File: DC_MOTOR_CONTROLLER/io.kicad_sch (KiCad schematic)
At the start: 12 parts, among them SW1 PEC12R, U1 NHD-C12832A1Z-FSRGB

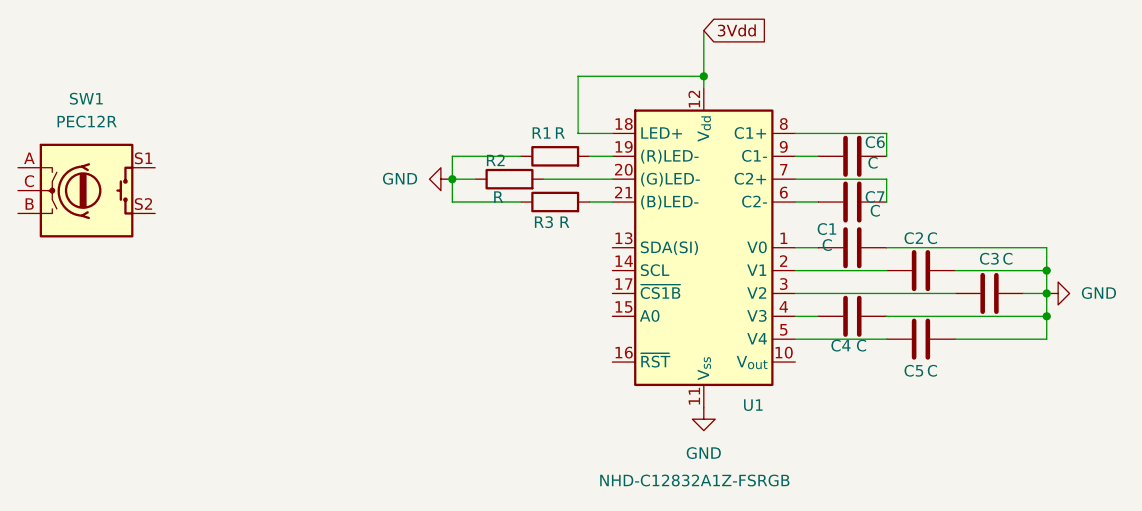
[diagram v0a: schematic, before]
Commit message: worked on h-bridge, pwm, io
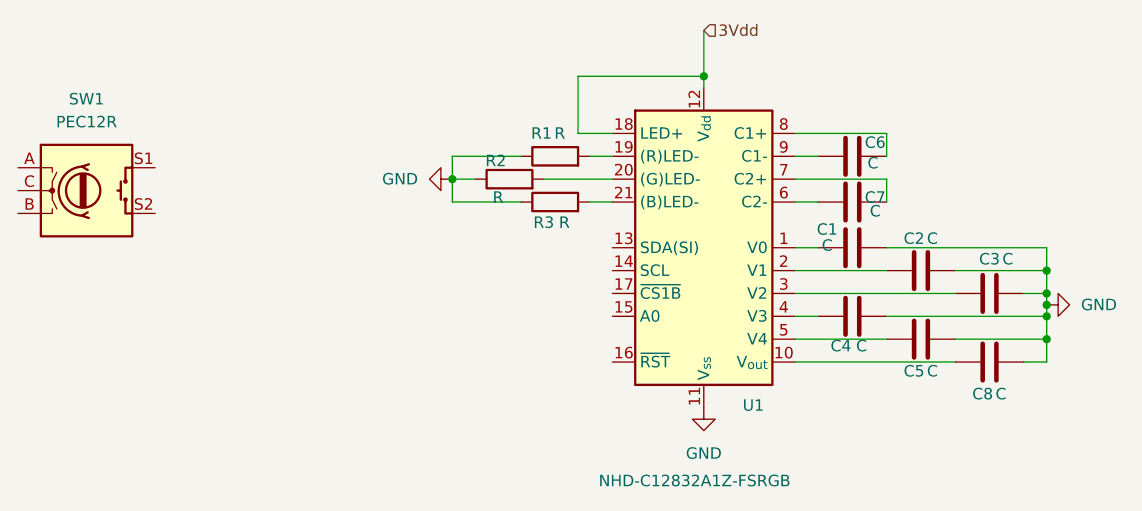
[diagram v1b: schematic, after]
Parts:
- added C8: C, symbol Device:C
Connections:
- net GND: now also C8.2
- net at U1.10 (V_{out}): now also C8.1
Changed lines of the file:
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@@
+	)
+	(junction
+		(at 190.5 80.01)
+		(diameter 0)
+		(color 0 0 0 0)
 	)
 	(junction
@@
 	)
 	(junction
+		(at 190.5 83.82)
+		(diameter 0)
+		(color 0 0 0 0)
+	)
+	(junction
 		(at 190.5 81.28)
 		(diameter 0)
@@
 	(wire
 		(pts
-			(xy 190.5 81.28) (xy 190.5 78.74)
+			(xy 190.5 81.28) (xy 190.5 80.01)
 		)
 		(stroke
@@
 	(wire
 		(pts
+			(xy 162.56 86.36) (xy 180.34 86.36)
+		)
+		(stroke
+			(width 0)
+			(type default)
+		)
+	)
+	(wire
+		(pts
+			(xy 190.5 86.36) (xy 190.5 83.82)
+		)
+		(stroke
+			(width 0)
+			(type default)
+		)
+	)
+	(wire
+		(pts
 			(xy 190.5 73.66) (xy 190.5 76.2)
 		)
@@
 	(wire
 		(pts
+			(xy 190.5 80.01) (xy 190.5 78.74)
+		)
+		(stroke
+			(width 0)
+			(type default)
+		)
+	)
+	(wire
+		(pts
 			(xy 152.4 54.61) (xy 152.4 55.88)
 		)
@@
 		)
 	)
-	(global_label "3Vdd"
+	(wire
+		(pts
+			(xy 187.96 86.36) (xy 190.5 86.36)
+		)
+		(stroke
+			(width 0)
+			(type default)
+		)
+	)
+	(hierarchical_label "3Vdd"
 		(shape input)
 		(at 152.4 49.53 0)
-		(fields_autoplaced yes)
 		(effects
 			(font
@@
 			)
 			(justify left)
-		)
-		(property "Intersheetrefs" "${INTERSHEET_REFS}"
-			(at 159.9813 49.53 0)
-			(effects
-				(font
-					(size 1.27 1.27)
-				)
-				(justify left)
-				(hide yes)
-			)
 		)
 	)
@@
 	)
 	(symbol
-		(lib_id "power:GND")
-		(at 190.5 78.74 90)
-		(unit 1)
-		(exclude_from_sim no)
-		(in_bom yes)
-		(on_board yes)
-		(dnp no)
-		(fields_autoplaced yes)
-		(property "Reference" "#PWR01"
-			(at 196.85 78.74 0)
-			(effects
-				(font
-					(size 1.27 1.27)
-				)
-				(hide yes)
-			)
-		)
-		(property "Value" "GND"
-			(at 194.31 78.7399 90)
-			(effects
-				(font
-					(size 1.27 1.27)
-				)
-				(justify right)
-			)
-		)
-		(property "Footprint" ""
-			(at 190.5 78.74 0)
-			(effects
-				(font
-					(size 1.27 1.27)
-				)
-				(hide yes)
-			)
-		)
-		(property "Datasheet" ""
-			(at 190.5 78.74 0)
-			(effects
-				(font
-					(size 1.27 1.27)
-				)
-				(hide yes)
-			)
-		)
-		(property "Description" "Power symbol creates a global label with name \"GND\" , ground"
-			(at 190.5 78.74 0)
-			(effects
-				(font
-					(size 1.27 1.27)
-				)
-				(hide yes)
-			)
-		)
-		(pin "1"
-		)
-		(instances
-			(project ""
-				(path "/4e267608-d3e9-4ae4-92d6-1e687cc2c969/818b61c9-cdb7-42ed-8a55-79736ba5dd65"
-					(reference "#PWR01")
-					(unit 1)
-				)
-			)
-		)
-	)
-	(symbol
 		(lib_id "Device:C")
 		(at 168.91 63.5 90)
@@
 				(path "/4e267608-d3e9-4ae4-92d6-1e687cc2c969/818b61c9-cdb7-42ed-8a55-79736ba5dd65"
 					(reference "C6")
+					(unit 1)
+				)
+			)
+		)
+	)
+	(symbol
+		(lib_id "Device:C")
+		(at 184.15 86.36 90)
+		(unit 1)
+		(exclude_from_sim no)
+		(in_bom yes)
+		(on_board yes)
+		(dnp no)
+		(property "Reference" "C8"
+			(at 183.388 89.916 90)
+			(effects
+				(font
+					(size 1.27 1.27)
+				)
+			)
+		)
+		(property "Value" "C"
+			(at 185.42 89.916 90)
+			(effects
+				(font
+					(size 1.27 1.27)
+				)
+			)
+		)
+		(property "Footprint" ""
+			(at 187.96 85.3948 0)
+			(effects
+				(font
+					(size 1.27 1.27)
+				)
+				(hide yes)
+			)
+		)
+		(property "Datasheet" "~"
+			(at 184.15 86.36 0)
+			(effects
+				(font
+					(size 1.27 1.27)
+				)
+				(hide yes)
+			)
+		)
+		(property "Description" "Unpolarized capacitor"
+			(at 184.15 86.36 0)
+			(effects
+				(font
+					(size 1.27 1.27)
+				)
+				(hide yes)
+			)
+		)
+		(pin "2"
+		)
+		(pin "1"
+		)
+		(instances
+			(project "DC_MOTOR_CONTROLLER"
+				(path "/4e267608-d3e9-4ae4-92d6-1e687cc2c969/818b61c9-cdb7-42ed-8a55-79736ba5dd65"
+					(reference "C8")
 					(unit 1)
 				)
@@
 					(unit 1)
 				)
+			)
+		)
+	)
+	(symbol
+		(lib_id "power:GND")
+		(at 190.5 80.01 90)
+		(unit 1)
+		(exclude_from_sim no)
+		(in_bom yes)
+		(on_board yes)
+		(dnp no)
+		(fields_autoplaced yes)
+		(property "Reference" "#PWR01"
+			(at 196.85 80.01 0)
+			(effects
+				(font
+					(size 1.27 1.27)
+				)
+				(hide yes)
+			)
+		)
+		(property "Value" "GND"
+			(at 194.31 80.0099 90)
+			(effects
+				(font
+					(size 1.27 1.27)
+				)
+				(justify right)
+			)
+		)
+		(property "Footprint" ""
+			(at 190.5 80.01 0)
+			(effects
+				(font
+					(size 1.27 1.27)
+				)
+				(hide yes)
+			)
+		)
+		(property "Datasheet" ""
+			(at 190.5 80.01 0)
+			(effects
+				(font
+					(size 1.27 1.27)
+				)
+				(hide yes)
+			)
+		)
+		(property "Description" "Power symbol creates a global label with name \"GND\" , ground"
+			(at 190.5 80.01 0)
+			(effects
+				(font
+					(size 1.27 1.27)
+				)
+				(hide yes)
+			)
+		)
+		(pin "1"
+		)
+		(instances
+			(project "DC_MOTOR_CONTROLLER"
+				(path "/4e267608-d3e9-4ae4-92d6-1e687cc2c969/818b61c9-cdb7-42ed-8a55-79736ba5dd65"
+					(reference "#PWR01")
+					(unit 1)
+				)
